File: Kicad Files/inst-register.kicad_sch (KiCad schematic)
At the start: 20 parts, among them U38 74LS245, U39 74LS173, U40 74LS173

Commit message: tidy up
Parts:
- renumbered C20 to C19, D95 to D79, D96 to D80, D97 to D81, D98 to D82, D99 to D83, D100 to D84, D101 to D85, D102 to D86, R104 to R88, R105 to R89, R106 to R90, R107 to R91, R108 to R92, R109 to R93, R110 to R94, R111 to R95, U38 to U32, U39 to U33, U40 to U34
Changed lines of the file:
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@@
   (symbol (lib_id "8bit-computer-rescue:LED_ALT-Device") (at 139.7 154.94 90) (unit 1)
     (in_bom yes) (on_board yes)
-    (property "Reference" "D99" (id 0) (at 137.16 154.94 0))
+    (property "Reference" "D83" (id 0) (at 137.16 154.94 0))
     (property "Value" "YELLOW" (id 1) (at 142.24 154.94 0))
     (property "Footprint" "LED_THT:LED_D5.0mm" (id 2) (at 139.7 154.94 0)
@@
   (symbol (lib_id "8bit-computer-rescue:LED_ALT-Device") (at 147.32 154.94 90) (unit 1)
     (in_bom yes) (on_board yes)
-    (property "Reference" "D100" (id 0) (at 144.78 154.94 0))
+    (property "Reference" "D84" (id 0) (at 144.78 154.94 0))
     (property "Value" "YELLOW" (id 1) (at 149.86 154.94 0))
     (property "Footprint" "LED_THT:LED_D5.0mm" (id 2) (at 147.32 154.94 0)
@@
   (symbol (lib_id "Device:R") (at 139.7 162.56 0) (unit 1)
     (in_bom yes) (on_board yes)
-    (property "Reference" "R108" (id 0) (at 141.732 162.56 90))
+    (property "Reference" "R92" (id 0) (at 141.732 162.56 90))
     (property "Value" "R" (id 1) (at 139.7 162.56 90))
     (property "Footprint" "Resistor_THT:R_Axial_DIN0207_L6.3mm_D2.5mm_P7.62mm_Horizontal" (id 2) (at 137.922 162.56 90)
@@
   (symbol (lib_id "power:GND") (at 91.44 107.95 0) (unit 1)
     (in_bom yes) (on_board yes)
-    (property "Reference" "#PWR087" (id 0) (at 91.44 114.3 0)
+    (property "Reference" "#PWR070" (id 0) (at 91.44 114.3 0)
       (effects (font (size 1.27 1.27)) hide)
     )
@@
   (symbol (lib_id "8bit-computer-rescue:74LS173-8bit-computer-rescue") (at 143.51 81.28 270) (unit 1)
     (in_bom yes) (on_board yes)
-    (property "Reference" "U39" (id 0) (at 146.05 83.82 0))
+    (property "Reference" "U33" (id 0) (at 146.05 83.82 0))
     (property "Value" "74LS173" (id 1) (at 142.24 83.82 0))
     (property "Footprint" "Package_DIP:DIP-16_W7.62mm" (id 2) (at 143.51 81.28 0)
@@
   (symbol (lib_id "8bit-computer-rescue:74LS173-8bit-computer-rescue") (at 184.15 81.28 270) (unit 1)
     (in_bom yes) (on_board yes)
-    (property "Reference" "U40" (id 0) (at 186.69 83.82 0))
+    (property "Reference" "U34" (id 0) (at 186.69 83.82 0))
     (property "Value" "74LS173" (id 1) (at 182.88 83.82 0))
     (property "Footprint" "Package_DIP:DIP-16_W7.62mm" (id 2) (at 184.15 81.28 0)
@@
   (symbol (lib_id "8bit-computer-rescue:74LS245-8bit-computer-rescue") (at 101.6 81.28 90) (unit 1)
     (in_bom yes) (on_board yes)
-    (property "Reference" "U38" (id 0) (at 86.995 78.74 0)
+    (property "Reference" "U32" (id 0) (at 86.995 78.74 0)
       (effects (font (size 1.27 1.27)) (justify left bottom))
     )
@@
   (symbol (lib_id "8bit-computer-rescue:LED_ALT-Device") (at 154.94 154.94 90) (unit 1)
     (in_bom yes) (on_board yes)
-    (property "Reference" "D101" (id 0) (at 152.4 154.94 0))
+    (property "Reference" "D85" (id 0) (at 152.4 154.94 0))
     (property "Value" "YELLOW" (id 1) (at 157.48 154.94 0))
     (property "Footprint" "LED_THT:LED_D5.0mm" (id 2) (at 154.94 154.94 0)
@@
   (symbol (lib_id "8bit-computer-rescue:LED_ALT-Device") (at 162.56 154.94 90) (unit 1)
     (in_bom yes) (on_board yes)
-    (property "Reference" "D102" (id 0) (at 160.02 154.94 0))
+    (property "Reference" "D86" (id 0) (at 160.02 154.94 0))
     (property "Value" "YELLOW" (id 1) (at 165.1 154.94 0))
     (property "Footprint" "LED_THT:LED_D5.0mm" (id 2) (at 162.56 154.94 0)
@@
   (symbol (lib_id "Device:R") (at 109.22 162.56 0) (unit 1)
     (in_bom yes) (on_board yes)
-    (property "Reference" "R104" (id 0) (at 111.252 162.56 90))
+    (property "Reference" "R88" (id 0) (at 111.252 162.56 90))
     (property "Value" "R" (id 1) (at 109.22 162.56 90))
     (property "Footprint" "Resistor_THT:R_Axial_DIN0207_L6.3mm_D2.5mm_P7.62mm_Horizontal" (id 2) (at 107.442 162.56 90)
@@
   (symbol (lib_id "Device:R") (at 116.84 162.56 0) (unit 1)
     (in_bom yes) (on_board yes)
-    (property "Reference" "R105" (id 0) (at 118.872 162.56 90))
+    (property "Reference" "R89" (id 0) (at 118.872 162.56 90))
     (property "Value" "R" (id 1) (at 116.84 162.56 90))
     (property "Footprint" "Resistor_THT:R_Axial_DIN0207_L6.3mm_D2.5mm_P7.62mm_Horizontal" (id 2) (at 115.062 162.56 90)
@@
   (symbol (lib_id "Device:R") (at 124.46 162.56 0) (unit 1)
     (in_bom yes) (on_board yes)
-    (property "Reference" "R106" (id 0) (at 126.492 162.56 90))
+    (property "Reference" "R90" (id 0) (at 126.492 162.56 90))
     (property "Value" "R" (id 1) (at 124.46 162.56 90))
     (property "Footprint" "Resistor_THT:R_Axial_DIN0207_L6.3mm_D2.5mm_P7.62mm_Horizontal" (id 2) (at 122.682 162.56 90)
@@
   (symbol (lib_id "Device:R") (at 132.08 162.56 0) (unit 1)
     (in_bom yes) (on_board yes)
-    (property "Reference" "R107" (id 0) (at 134.112 162.56 90))
+    (property "Reference" "R91" (id 0) (at 134.112 162.56 90))
     (property "Value" "R" (id 1) (at 132.08 162.56 90))
     (property "Footprint" "Resistor_THT:R_Axial_DIN0207_L6.3mm_D2.5mm_P7.62mm_Horizontal" (id 2) (at 130.302 162.56 90)
@@
   (symbol (lib_id "Device:R") (at 147.32 162.56 0) (unit 1)
     (in_bom yes) (on_board yes)
-    (property "Reference" "R109" (id 0) (at 149.352 162.56 90))
+    (property "Reference" "R93" (id 0) (at 149.352 162.56 90))
     (property "Value" "R" (id 1) (at 147.32 162.56 90))
     (property "Footprint" "Resistor_THT:R_Axial_DIN0207_L6.3mm_D2.5mm_P7.62mm_Horizontal" (id 2) (at 145.542 162.56 90)
@@
   (symbol (lib_id "Device:R") (at 154.94 162.56 0) (unit 1)
     (in_bom yes) (on_board yes)
-    (property "Reference" "R110" (id 0) (at 156.972 162.56 90))
+    (property "Reference" "R94" (id 0) (at 156.972 162.56 90))
     (property "Value" "R" (id 1) (at 154.94 162.56 90))
     (property "Footprint" "Resistor_THT:R_Axial_DIN0207_L6.3mm_D2.5mm_P7.62mm_Horizontal" (id 2) (at 153.162 162.56 90)
@@
   (symbol (lib_id "Device:R") (at 162.56 162.56 0) (unit 1)
     (in_bom yes) (on_board yes)
-    (property "Reference" "R111" (id 0) (at 164.592 162.56 90))
+    (property "Reference" "R95" (id 0) (at 164.592 162.56 90))
     (property "Value" "R" (id 1) (at 162.56 162.56 90))
     (property "Footprint" "Resistor_THT:R_Axial_DIN0207_L6.3mm_D2.5mm_P7.62mm_Horizontal" (id 2) (at 160.782 162.56 90)
@@
   (symbol (lib_id "power:GND") (at 135.89 166.37 0) (unit 1)
     (in_bom yes) (on_board yes)
-    (property "Reference" "#PWR089" (id 0) (at 135.89 172.72 0)
+    (property "Reference" "#PWR072" (id 0) (at 135.89 172.72 0)
       (effects (font (size 1.27 1.27)) hide)
     )
@@
   (symbol (lib_id "power:VCC") (at 111.76 99.06 180) (unit 1)
     (in_bom yes) (on_board yes)
-    (property "Reference" "#PWR088" (id 0) (at 111.76 95.25 0)
+    (property "Reference" "#PWR071" (id 0) (at 111.76 95.25 0)
       (effects (font (size 1.27 1.27)) hide)
     )
@@
   (symbol (lib_id "power:GND") (at 205.74 68.58 0) (unit 1)
     (in_bom yes) (on_board yes)
-    (property "Reference" "#PWR090" (id 0) (at 205.74 74.93 0)
+    (property "Reference" "#PWR073" (id 0) (at 205.74 74.93 0)
       (effects (font (size 1.27 1.27)) hide)
     )
@@
   (symbol (lib_id "Device:C") (at 64.77 88.9 0) (unit 1)
     (in_bom yes) (on_board yes)
-    (property "Reference" "C20" (id 0) (at 65.405 86.36 0)
+    (property "Reference" "C19" (id 0) (at 65.405 86.36 0)
       (effects (font (size 1.27 1.27)) (justify left))
     )
@@
   (symbol (lib_id "power:GND") (at 64.77 95.25 0) (unit 1)
     (in_bom yes) (on_board yes)
-    (property "Reference" "#PWR086" (id 0) (at 64.77 101.6 0)
+    (property "Reference" "#PWR069" (id 0) (at 64.77 101.6 0)
       (effects (font (size 1.27 1.27)) hide)
     )
@@
   (symbol (lib_id "power:VCC") (at 64.77 82.55 0) (unit 1)
     (in_bom yes) (on_board yes)
-    (property "Reference" "#PWR085" (id 0) (at 64.77 86.36 0)
+    (property "Reference" "#PWR068" (id 0) (at 64.77 86.36 0)
       (effects (font (size 1.27 1.27)) hide)
     )
@@
   (symbol (lib_id "8bit-computer-rescue:LED_ALT-Device") (at 109.22 154.94 90) (unit 1)
     (in_bom yes) (on_board yes)
-    (property "Reference" "D95" (id 0) (at 106.68 154.94 0))
+    (property "Reference" "D79" (id 0) (at 106.68 154.94 0))
     (property "Value" "YELLOW" (id 1) (at 111.76 154.94 0))
     (property "Footprint" "LED_THT:LED_D5.0mm" (id 2) (at 109.22 154.94 0)
@@
   (symbol (lib_id "8bit-computer-rescue:LED_ALT-Device") (at 116.84 154.94 90) (unit 1)
     (in_bom yes) (on_board yes)
-    (property "Reference" "D96" (id 0) (at 114.3 154.94 0))
+    (property "Reference" "D80" (id 0) (at 114.3 154.94 0))
     (property "Value" "YELLOW" (id 1) (at 119.38 154.94 0))
     (property "Footprint" "LED_THT:LED_D5.0mm" (id 2) (at 116.84 154.94 0)
@@
   (symbol (lib_id "8bit-computer-rescue:LED_ALT-Device") (at 124.46 154.94 90) (unit 1)
     (in_bom yes) (on_board yes)
-    (property "Reference" "D97" (id 0) (at 121.92 154.94 0))
+    (property "Reference" "D81" (id 0) (at 121.92 154.94 0))
     (property "Value" "YELLOW" (id 1) (at 127 154.94 0))
     (property "Footprint" "LED_THT:LED_D5.0mm" (id 2) (at 124.46 154.94 0)
@@
   (symbol (lib_id "8bit-computer-rescue:LED_ALT-Device") (at 132.08 154.94 90) (unit 1)
     (in_bom yes) (on_board yes)
-    (property "Reference" "D98" (id 0) (at 129.54 154.94 0))
+    (property "Reference" "D82" (id 0) (at 129.54 154.94 0))
     (property "Value" "YELLOW" (id 1) (at 134.62 154.94 0))
     (property "Footprint" "LED_THT:LED_D5.0mm" (id 2) (at 132.08 154.94 0)

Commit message: updated library
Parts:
- removed D79, D80, D81, D82, D83, D84, D85, D86: YELLOW, LED_THT:LED_D5.0mm, symbol 8bit-computer-rescue:LED_ALT-Device
- removed R88, R89, R90, R91, R92, R93, R94, R95: R, Resistor_THT:R_Axial_DIN0207_L6.3mm_D2.5mm_P7.62mm_Horizontal, symbol Device:R
- removed U32: 74LS245, Package_DIP:DIP-20_W7.62mm, symbol 8bit-computer-rescue:74LS245-8bit-computer-rescue
- removed U33, U34: 74LS173, Package_DIP:DIP-16_W7.62mm, symbol 8bit-computer-rescue:74LS173-8bit-computer-rescue
- added D87, D88, D89, D90, D91, D92, D93, D94: LED, symbol Device:LED
- added R100, R101, R102, R103, R96, R97, R98, R99: R_Small, symbol Device:R_Small
- added U32: 74HC245, symbol 74xx:74HC245
- added U33, U34: 74LS173, symbol 74xx:74LS173
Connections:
- net BUS_0: now also U32.11 (B7), U34.11 (D3)
- net BUS_1: now also U32.12 (B6), U34.12 (D2)
- net BUS_2: now also U32.13 (B5), U34.13 (D1)
- net BUS_3: now also U32.14 (B4), U34.14 (D0)
- net BUS_4: now also U32.15 (B3), U33.11 (D3)
- net BUS_5: now also U32.16 (B2), U33.12 (D2)
- net BUS_6: now also U32.17 (B1), U33.13 (D1)
- net BUS_7: now also U32.18 (B0), U33.14 (D0)
- net CLK: now also U33.7 (Cp), U34.7 (Cp)
- net CLR: now also U33.15 (Mr), U34.15 (Mr)
- net GND: now also R100.2, R101.2, R102.2, R103.2, R96.2, R97.2, R98.2, R99.2, U32.10 (GND), U33.1 (Oe1), U33.16 (VCC), U33.2 (Oe2), U34.1 (Oe1), U34.16 (VCC), U34.2 (Oe2)
- net IR_0: now also D94.2 (A), U32.9 (A7), U34.6 (Q3)
- net IR_1: now also D93.2 (A), U32.8 (A6), U34.5 (Q2)
- net IR_2: now also D92.2 (A), U32.7 (A5), U34.4 (Q1)
- net IR_3: now also D91.2 (A), U32.6 (A4), U34.3 (Q0)
- net IR_4: now also D90.2 (A), U32.5 (A3), U33.6 (Q3)
- net IR_5: now also D89.2 (A), U32.4 (A2), U33.5 (Q2)
- net IR_6: now also D88.2 (A), U32.3 (A1), U33.4 (Q1)
- net IR_7: now also D87.2 (A), U32.2 (A0), U33.3 (Q0)
- net VCC: now also U32.1 (A->B), U32.20 (VCC), U33.8 (GND), U34.8 (GND)
- net ~{II}: now also U33.10 (E2), U33.9 (E1), U34.10 (E2), U34.9 (E1)
- net ~{IO}: now also U32.19 (CE)
- new net: D93.1 (K), R102.1
- new net: D87.1 (K), R96.1
- new net: D94.1 (K), R103.1
- new net: D91.1 (K), R100.1
- new net: D92.1 (K), R101.1
- new net: D88.1 (K), R97.1
- new net: D89.1 (K), R98.1
- new net: D90.1 (K), R99.1
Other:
- moved on the sheet: C19

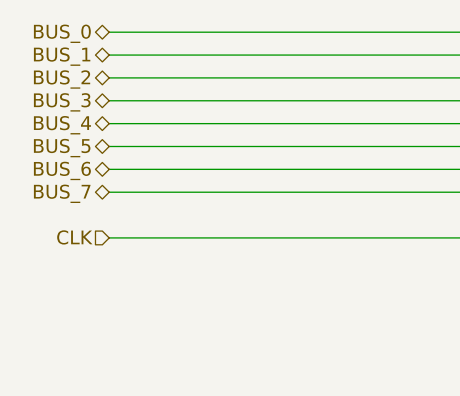
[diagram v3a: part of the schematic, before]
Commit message: complete redraw to bus system
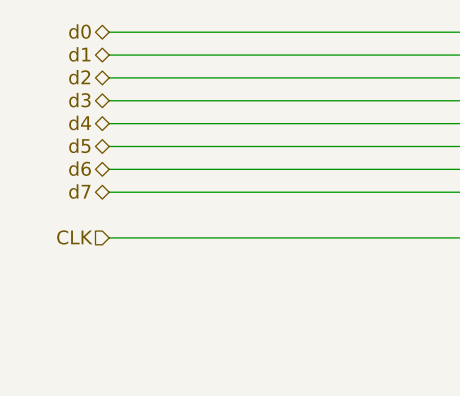
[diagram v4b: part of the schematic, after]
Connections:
- net BUS_0 renamed d0
- net BUS_1 renamed d1
- net BUS_2 renamed d2
- net BUS_3 renamed d3
- net BUS_4 renamed d4
- net BUS_5 renamed d5
- net BUS_6 renamed d6
- net BUS_7 renamed d7
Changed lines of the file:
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@@
     (effects (font (size 1.524 1.524)) (justify right))
   )
-  (hierarchical_label "BUS_1" (shape bidirectional) (at 59.69 43.815 180)
-    (effects (font (size 1.524 1.524)) (justify right))
-  )
-  (hierarchical_label "BUS_3" (shape bidirectional) (at 59.69 48.895 180)
+  (hierarchical_label "d3" (shape tri_state) (at 59.69 48.895 180)
     (effects (font (size 1.524 1.524)) (justify right))
   )
@@
     (effects (font (size 1.524 1.524)) (justify left))
   )
-  (hierarchical_label "BUS_2" (shape bidirectional) (at 59.69 46.355 180)
+  (hierarchical_label "d4" (shape tri_state) (at 59.69 51.435 180)
     (effects (font (size 1.524 1.524)) (justify right))
   )
@@
     (effects (font (size 1.524 1.524)) (justify left))
   )
-  (hierarchical_label "BUS_5" (shape bidirectional) (at 59.69 53.975 180)
+  (hierarchical_label "d5" (shape tri_state) (at 59.69 53.975 180)
     (effects (font (size 1.524 1.524)) (justify right))
   )
-  (hierarchical_label "BUS_4" (shape bidirectional) (at 59.69 51.435 180)
+  (hierarchical_label "d1" (shape tri_state) (at 59.69 43.815 180)
+    (effects (font (size 1.524 1.524)) (justify right))
+  )
+  (hierarchical_label "d0" (shape tri_state) (at 59.69 41.275 180)
     (effects (font (size 1.524 1.524)) (justify right))
   )
@@
     (effects (font (size 1.524 1.524)) (justify left))
   )
+  (hierarchical_label "d6" (shape tri_state) (at 59.69 56.515 180)
+    (effects (font (size 1.524 1.524)) (justify right))
+  )
   (hierarchical_label "IR_6" (shape output) (at 124.206 158.369 0)
     (effects (font (size 1.524 1.524)) (justify left))
@@
     (effects (font (size 1.524 1.524)) (justify left))
   )
-  (hierarchical_label "BUS_0" (shape bidirectional) (at 59.69 41.275 180)
+  (hierarchical_label "d7" (shape tri_state) (at 59.69 59.055 180)
     (effects (font (size 1.524 1.524)) (justify right))
   )
-  (hierarchical_label "BUS_7" (shape bidirectional) (at 59.69 59.055 180)
+  (hierarchical_label "d2" (shape tri_state) (at 59.69 46.355 180)
     (effects (font (size 1.524 1.524)) (justify right))
   )
@@
     (effects (font (size 1.524 1.524)) (justify left))
   )
-  (hierarchical_label "BUS_6" (shape bidirectional) (at 59.69 56.515 180)
-    (effects (font (size 1.524 1.524)) (justify right))
-  )
   (hierarchical_label "IR_4" (shape output) (at 124.206 153.289 0)
